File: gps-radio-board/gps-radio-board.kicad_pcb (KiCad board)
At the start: 4 copper layers, 25 x 54 mm, 42 parts, among them J1 SMA, J2 SMA, J3 USB_C_Receptacle_USB2.0_16P, J4 JST_BATT, J5 Conn_01x04, J6 Conn_01x04, J7 Conn_01x04, U1 ESP32-C6-MINI-1U-H4, U4 AP2112K-3.3, U5 MAX-M10N, U6 MCP73831, U7 AP2112K-3.3

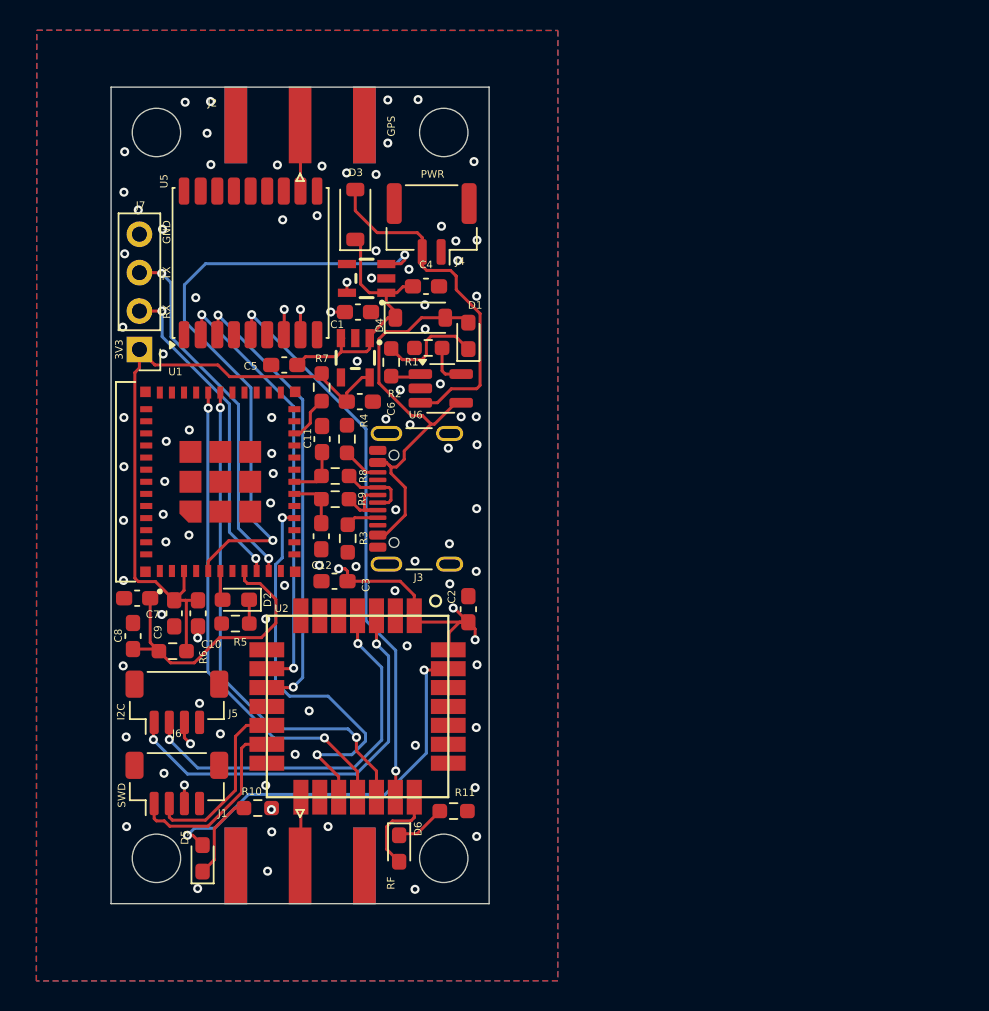
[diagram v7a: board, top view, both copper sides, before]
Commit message: Add active gps antenna circuit
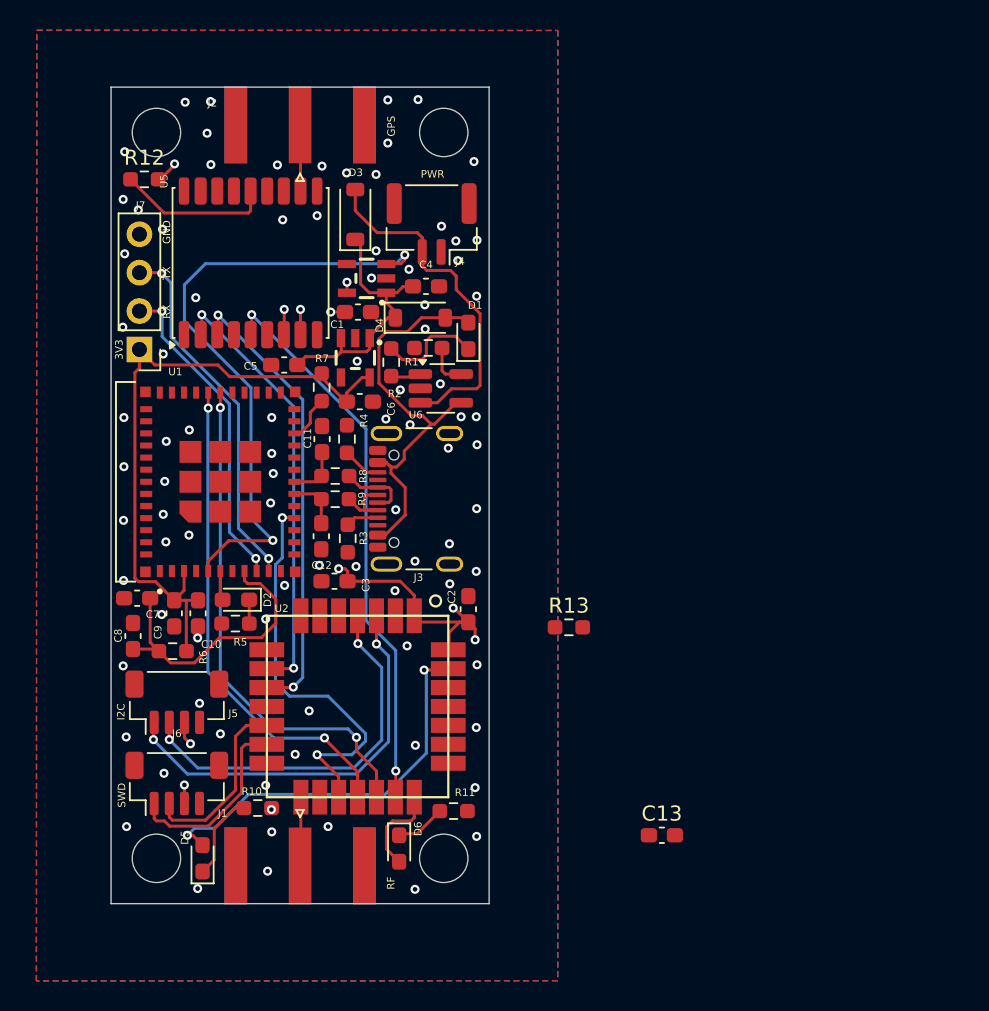
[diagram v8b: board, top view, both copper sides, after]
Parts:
- added C13: 100n, Capacitor_SMD:C_0603_1608Metric_Pad1.08x0.95mm_HandSolder, F.Cu at (123.9, 122.5)
- added R12: 0, Resistor_SMD:R_0603_1608Metric_Pad0.98x0.95mm_HandSolder, F.Cu at (89.7, 79.1)
- added R13: 100k, Resistor_SMD:R_0603_1608Metric_Pad0.98x0.95mm_HandSolder, F.Cu at (117.8, 108.7)
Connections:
- U2 pad 25: unconnected-(U2-PB9-Pad25) -> Net-(U2-PB9)
- U5 pad 13: unconnected-(U5-LNA_EN-Pad13) -> Net-(U2-PB9)
- U5 pad 14: unconnected-(U5-VCC_RF-Pad14) -> Net-(U5-VCC_RF)
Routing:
- net Net-(U5-VCC_RF): track 0.00 -> 10.2 mm
- net +3V3: track 24.7 -> 26.2 mm, vias 9 -> 10
